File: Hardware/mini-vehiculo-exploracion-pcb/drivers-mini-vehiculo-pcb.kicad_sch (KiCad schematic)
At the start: 18 parts, among them U3 DRV8873HPWPRQ1, U4 DRV8873HPWPRQ1

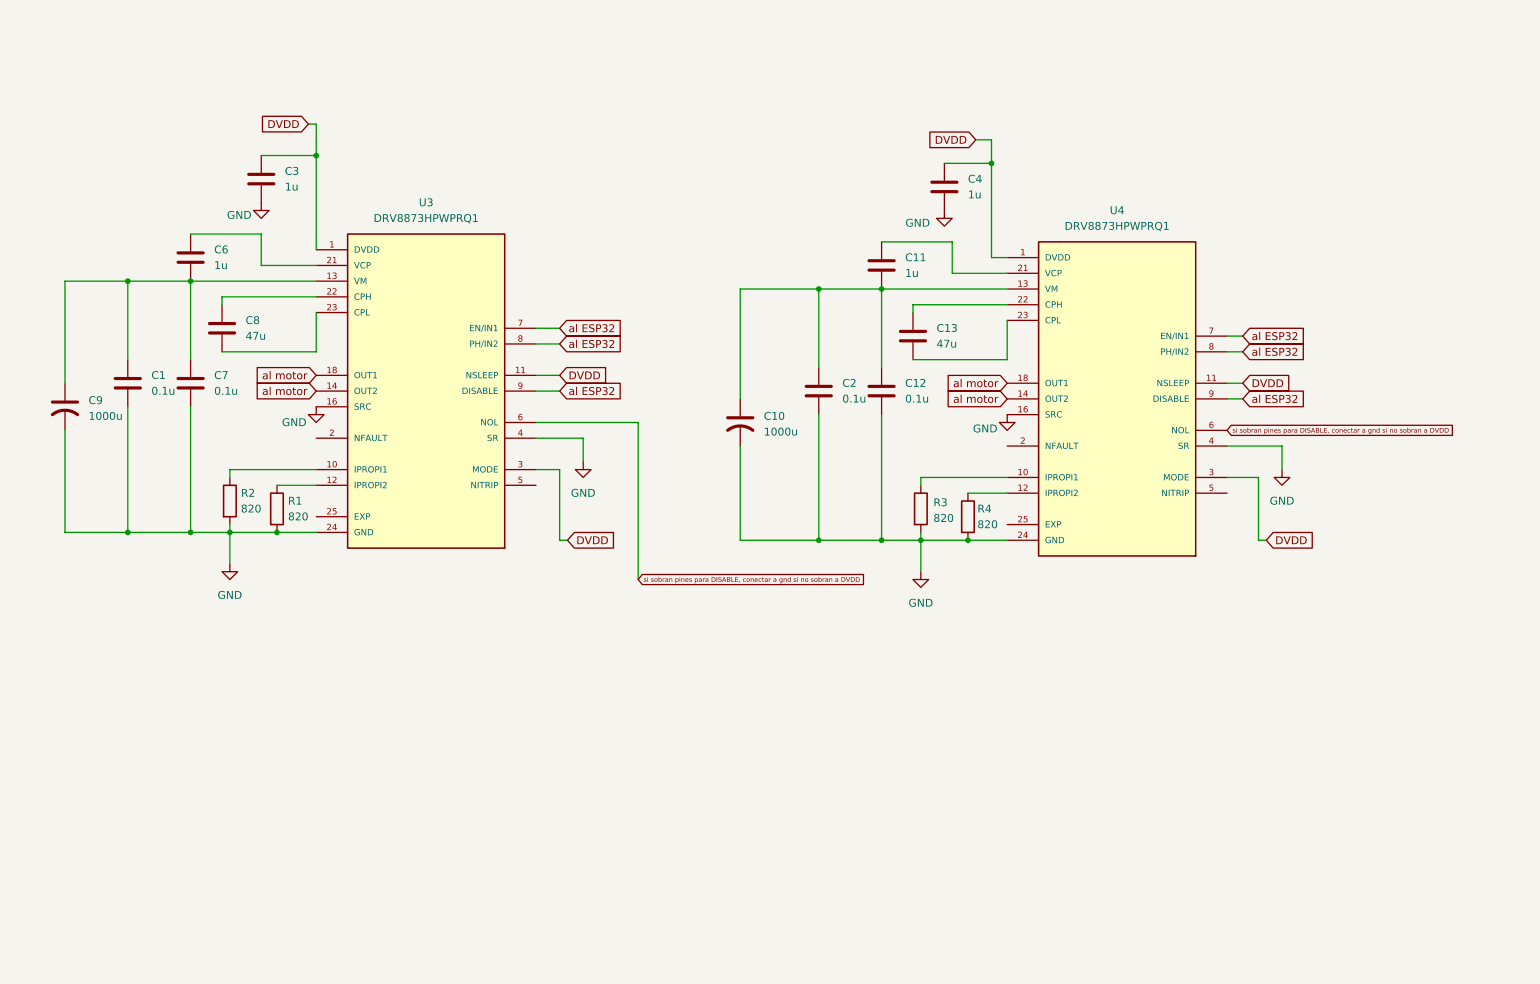
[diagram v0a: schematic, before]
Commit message: add driver pin labels
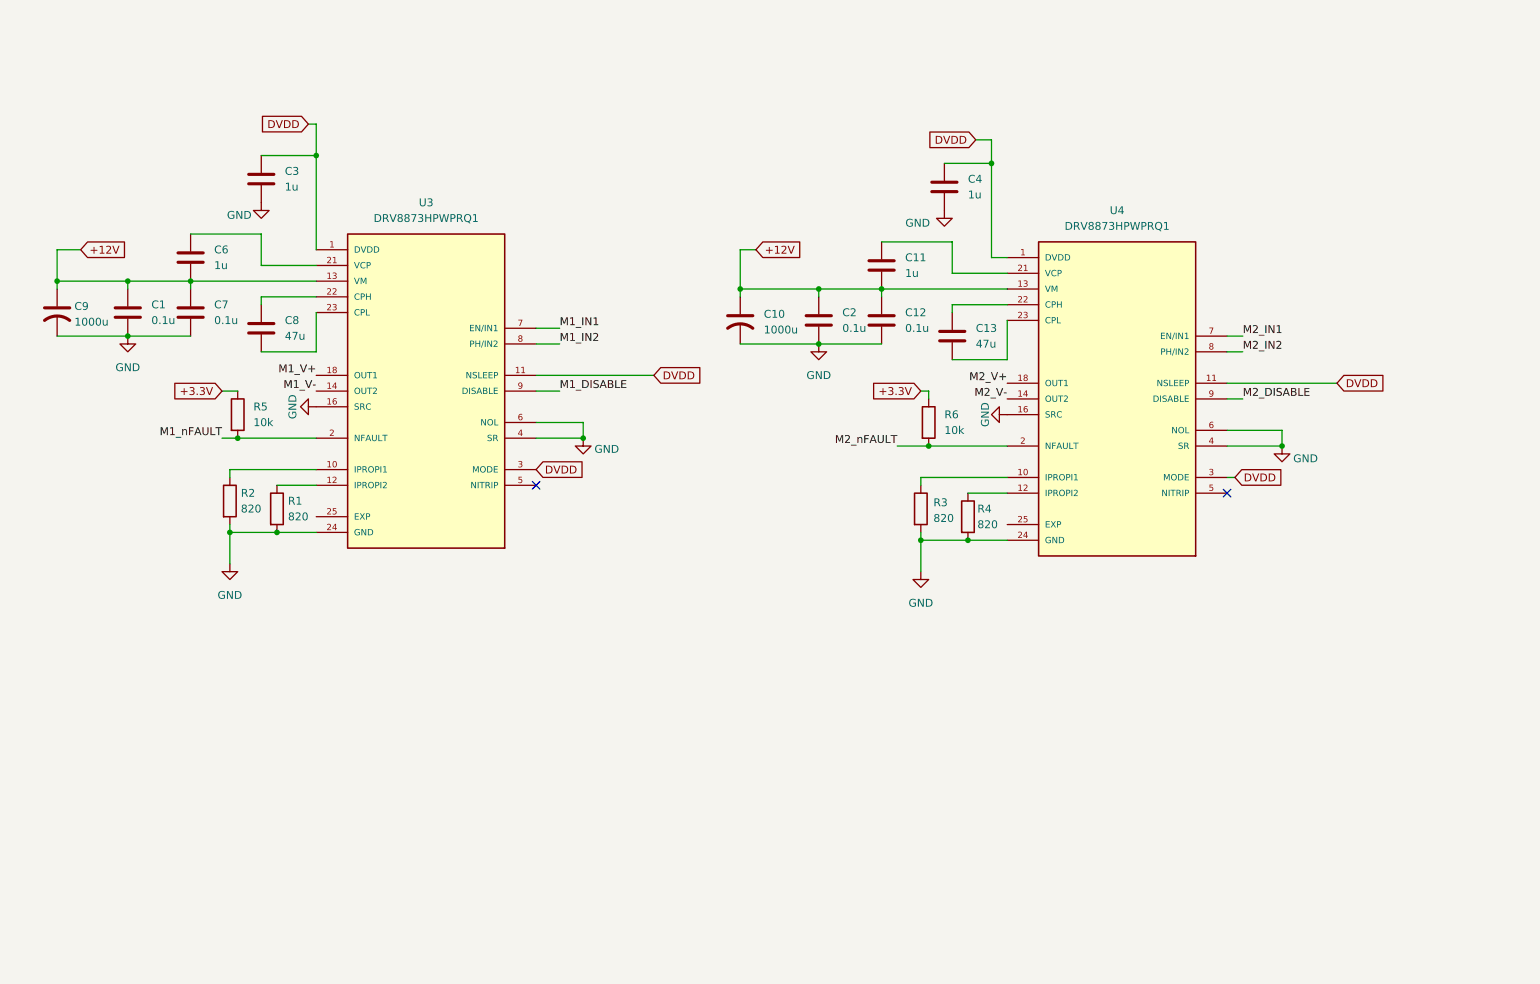
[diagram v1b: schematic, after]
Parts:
- added R5, R6: 10k, symbol Device:R
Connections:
- net si sobran pines para DISABLE, conectar a gnd si no sobran a DVDD is gone; now on net GND: U3.6 (NOL), U4.6 (NOL)
- net M1_nFAULT: now reaches U3.2 (NFAULT)
- net M1_nFAULT: now also R5.2
- net M2_nFAULT: now reaches U4.2 (NFAULT)
- net M2_nFAULT: now also R6.2
- removed net al ESP32: U3.7 (EN/IN1), U3.8 (PH/IN2), U3.9 (DISABLE), U4.7 (EN/IN1), U4.8 (PH/IN2), U4.9 (DISABLE)
- removed net al motor: U3.14 (OUT2), U3.15 (OUT2), U3.18 (OUT1), U3.19 (OUT1), U4.14 (OUT2), U4.15 (OUT2), U4.18 (OUT1), U4.19 (OUT1)
- new net +3.3V: R5.1, R6.1
- new net M1_DISABLE: U3.9 (DISABLE)
- new net M1_IN1: U3.7 (EN/IN1)
- new net M1_IN2: U3.8 (PH/IN2)
- new net M1_V+: U3.18 (OUT1), U3.19 (OUT1)
- new net M1_V-: U3.14 (OUT2), U3.15 (OUT2)
- new net M2_DISABLE: U4.9 (DISABLE)
- new net M2_IN1: U4.7 (EN/IN1)
- new net M2_IN2: U4.8 (PH/IN2)
- new net M2_V+: U4.18 (OUT1), U4.19 (OUT1)
- new net M2_V-: U4.14 (OUT2), U4.15 (OUT2)
- no-connect marks 0 -> 2
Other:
- moved on the sheet: C1, C10, C12, C13, C2, C7, C8, C9

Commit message: Update drivers-mini-vehiculo-pcb.kicad_sch
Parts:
- added J1: IO7, symbol Connector:Conn_01x01_Pin
- added J10, J12, J14, J16, J2, J4, J6, J8: GND_PIN, symbol Connector:Conn_01x01_Pin
- added J11: IO15, symbol Connector:Conn_01x01_Pin
- added J13: IO16, symbol Connector:Conn_01x01_Pin
- added J15: IO38, symbol Connector:Conn_01x01_Pin
- added J3: IO8, symbol Connector:Conn_01x01_Pin
- added J5: IO9, symbol Connector:Conn_01x01_Pin
- added J7: IO21, symbol Connector:Conn_01x01_Pin
- added J9: IO14, symbol Connector:Conn_01x01_Pin
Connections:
- net GND: now also J10.1 (Pin_1), J12.1 (Pin_1), J14.1 (Pin_1), J16.1 (Pin_1), J2.1 (Pin_1), J4.1 (Pin_1), J6.1 (Pin_1), J8.1 (Pin_1)
- net M1_DISABLE: now also J5.1 (Pin_1)
- net M1_IN1: now also J1.1 (Pin_1)
- net M1_IN2: now also J3.1 (Pin_1)
- net M1_nFAULT: now also J7.1 (Pin_1)
- net M2_DISABLE: now also J13.1 (Pin_1)
- net M2_IN1: now also J9.1 (Pin_1)
- net M2_IN2: now also J11.1 (Pin_1)
- net M2_nFAULT: now also J15.1 (Pin_1)
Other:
- note added: "Conectores al ESP32"
- note added: "DRIVER MOTOR 1"
- note added: "DRIVER MOTOR 2"
- moved on the sheet: C1, C10, C11, C12, C13, C2, C3, C4, C6, C7, C8, C9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

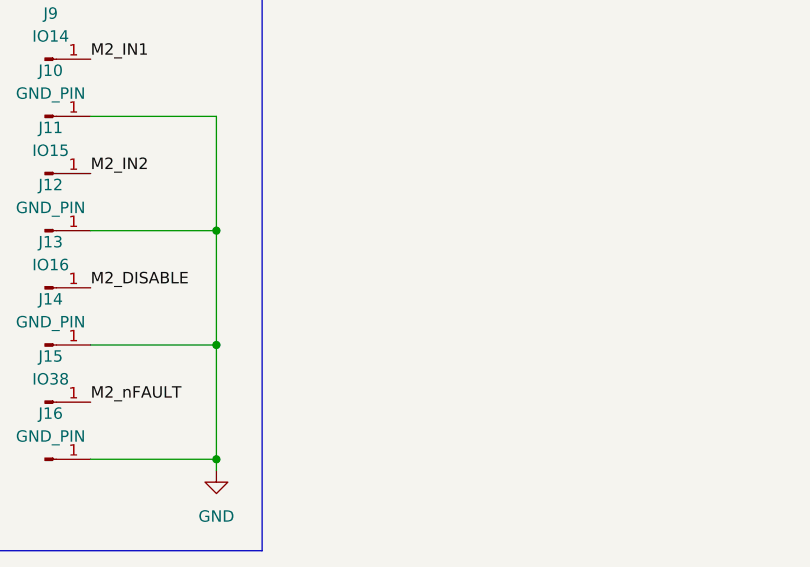
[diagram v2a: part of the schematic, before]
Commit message: update componentes
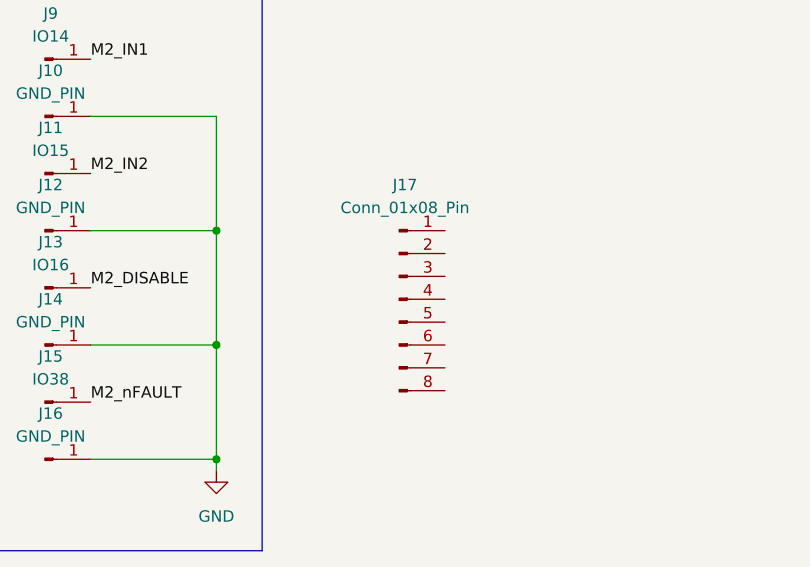
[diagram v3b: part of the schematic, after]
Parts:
- added J17: Conn_01x08_Pin, symbol Connector:Conn_01x08_Pin
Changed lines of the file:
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@@
+	)
+	(symbol
+		(lib_id "Connector:Conn_01x08_Pin")
+		(at 106.68 158.75 0)
+		(unit 1)
+		(exclude_from_sim no)
+		(in_bom yes)
+		(on_board yes)
+		(dnp no)
+		(fields_autoplaced yes)
+		(property "Reference" "J17"
+			(at 107.315 146.05 0)
+			(effects
+				(font
+					(size 1.27 1.27)
+				)
+			)
+		)
+		(property "Value" "Conn_01x08_Pin"
+			(at 107.315 148.59 0)
+			(effects
+				(font
+					(size 1.27 1.27)
+				)
+			)
+		)
+		(property "Footprint" ""
+			(at 106.68 158.75 0)
+			(effects
+				(font
+					(size 1.27 1.27)
+				)
+				(hide yes)
+			)
+		)
+		(property "Datasheet" "~"
+			(at 106.68 158.75 0)
+			(effects
+				(font
+					(size 1.27 1.27)
+				)
+				(hide yes)
+			)
+		)
+		(property "Description" "Generic connector, single row, 01x08, script generated"
+			(at 106.68 158.75 0)
+			(effects
+				(font
+					(size 1.27 1.27)
+				)
+				(hide yes)
+			)
+		)
+		(pin "8"
+		)
+		(pin "2"
+		)
+		(pin "6"
+		)
+		(pin "5"
+		)
+		(pin "4"
+		)
+		(pin "7"
+		)
+		(pin "3"
+		)
+		(pin "1"
+		)
+		(instances
+			(project ""
+				(path "/7776e3ee-622a-4a3e-a213-279f6f5df2cb"
+					(reference "J17")
+					(unit 1)
+				)
+			)
+		)
 	)
 	(symbol

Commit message: updated connectors for driver
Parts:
- removed J1: IO7, symbol Connector:Conn_01x01_Pin
- removed J10, J12, J14, J16, J2, J4, J6, J8: GND_PIN, symbol Connector:Conn_01x01_Pin
- removed J11: IO15, symbol Connector:Conn_01x01_Pin
- removed J13: IO16, symbol Connector:Conn_01x01_Pin
- removed J15: IO38, symbol Connector:Conn_01x01_Pin
- removed J17: Conn_01x08_Pin, symbol Connector:Conn_01x08_Pin
- removed J3: IO8, symbol Connector:Conn_01x01_Pin
- removed J5: IO9, symbol Connector:Conn_01x01_Pin
- removed J7: IO21, symbol Connector:Conn_01x01_Pin
- removed J9: IO14, symbol Connector:Conn_01x01_Pin
- added J1: Conn_01x08_Pin_drv, symbol ConectorDriverESP:Conn_01x08_Pin_drv
- added J2: Conn_01x02_Pin, symbol Connector:Conn_01x02_Pin
- added J3: Conn_01x02_Motor1, symbol Connector:Conn_01x02_Pin
- added J4: Conn_01x02_Motor2, symbol Connector:Conn_01x02_Pin
- added J5: Conn_01x02_Battery, symbol Connector:Conn_01x02_Pin
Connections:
- net GND: now also J1.8 (Pin_8), J5.2 (Pin_2)
- net M1_DISABLE: now also J1.3 (Pin_3), J2.1 (Pin_1)
- net M1_IN1: now also J1.1 (Pin_1)
- net M1_IN2: now also J1.2 (Pin_2)
- net M1_V+: now also J3.1 (Pin_1)
- net M1_V-: now also J3.2 (Pin_2)
- net M2_DISABLE: now also J1.7 (Pin_7), J2.2 (Pin_2)
- net M2_IN1: now also J1.5 (Pin_5)
- net M2_IN2: now also J1.6 (Pin_6)
- net M2_V+: now also J4.1 (Pin_1)
- net M2_V-: now also J4.2 (Pin_2)
- net VM: now also J5.1 (Pin_1)
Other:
- note added: "Bateria 12V"
- note added: "Conectores a los Motores"

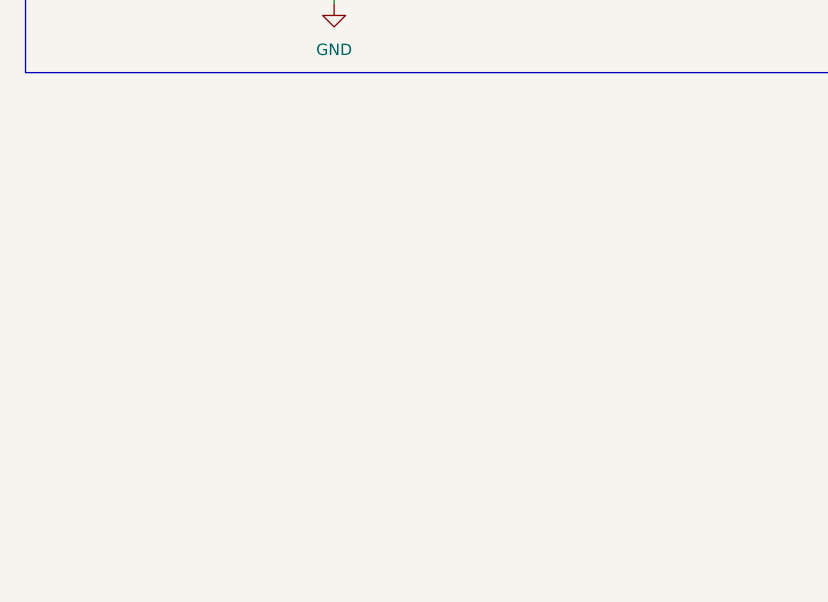
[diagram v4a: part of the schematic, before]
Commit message: carga librerias pcb de drivers
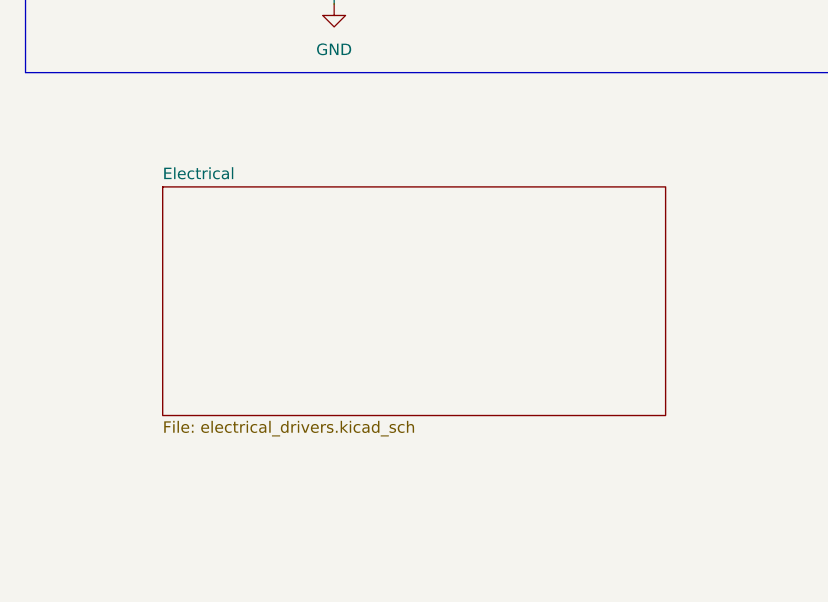
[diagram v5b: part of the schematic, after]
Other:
- added sheet Electrical (electrical_drivers.kicad_sch)
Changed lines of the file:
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@@
+		)
+	)
+	(sheet
+		(at 153.67 132.08)
+		(size 55.88 25.4)
+		(exclude_from_sim no)
+		(in_bom yes)
+		(on_board yes)
+		(dnp no)
+		(fields_autoplaced yes)
+		(stroke
+			(width 0.1524)
+			(type solid)
+		)
+		(fill
+			(color 0 0 0 0.0000)
+		)
+		(property "Sheetname" "Electrical"
+			(at 153.67 131.3684 0)
+			(effects
+				(font
+					(size 1.27 1.27)
+				)
+				(justify left bottom)
+			)
+		)
+		(property "Sheetfile" "electrical_drivers.kicad_sch"
+			(at 153.67 158.0646 0)
+			(effects
+				(font
+					(size 1.27 1.27)
+				)
+				(justify left top)
+			)
+		)
+		(instances
+			(project "drivers-mini-vehiculo-pcb"
+				(path "/7776e3ee-622a-4a3e-a213-279f6f5df2cb"
+					(page "2")
+				)
+			)
 		)
 	)
